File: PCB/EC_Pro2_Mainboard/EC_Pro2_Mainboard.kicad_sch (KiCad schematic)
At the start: 27 parts, among them J1 JST, J2 RGB, SW1 BOOT0, U1 STM32F401CBUx, U2 XC6206PxxxMR, U6 SN74AHCT1G125, Y1 8 MHz

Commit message: Updated sheets
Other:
- company: Cipulot PCB Design  -> LU.SV Solutions

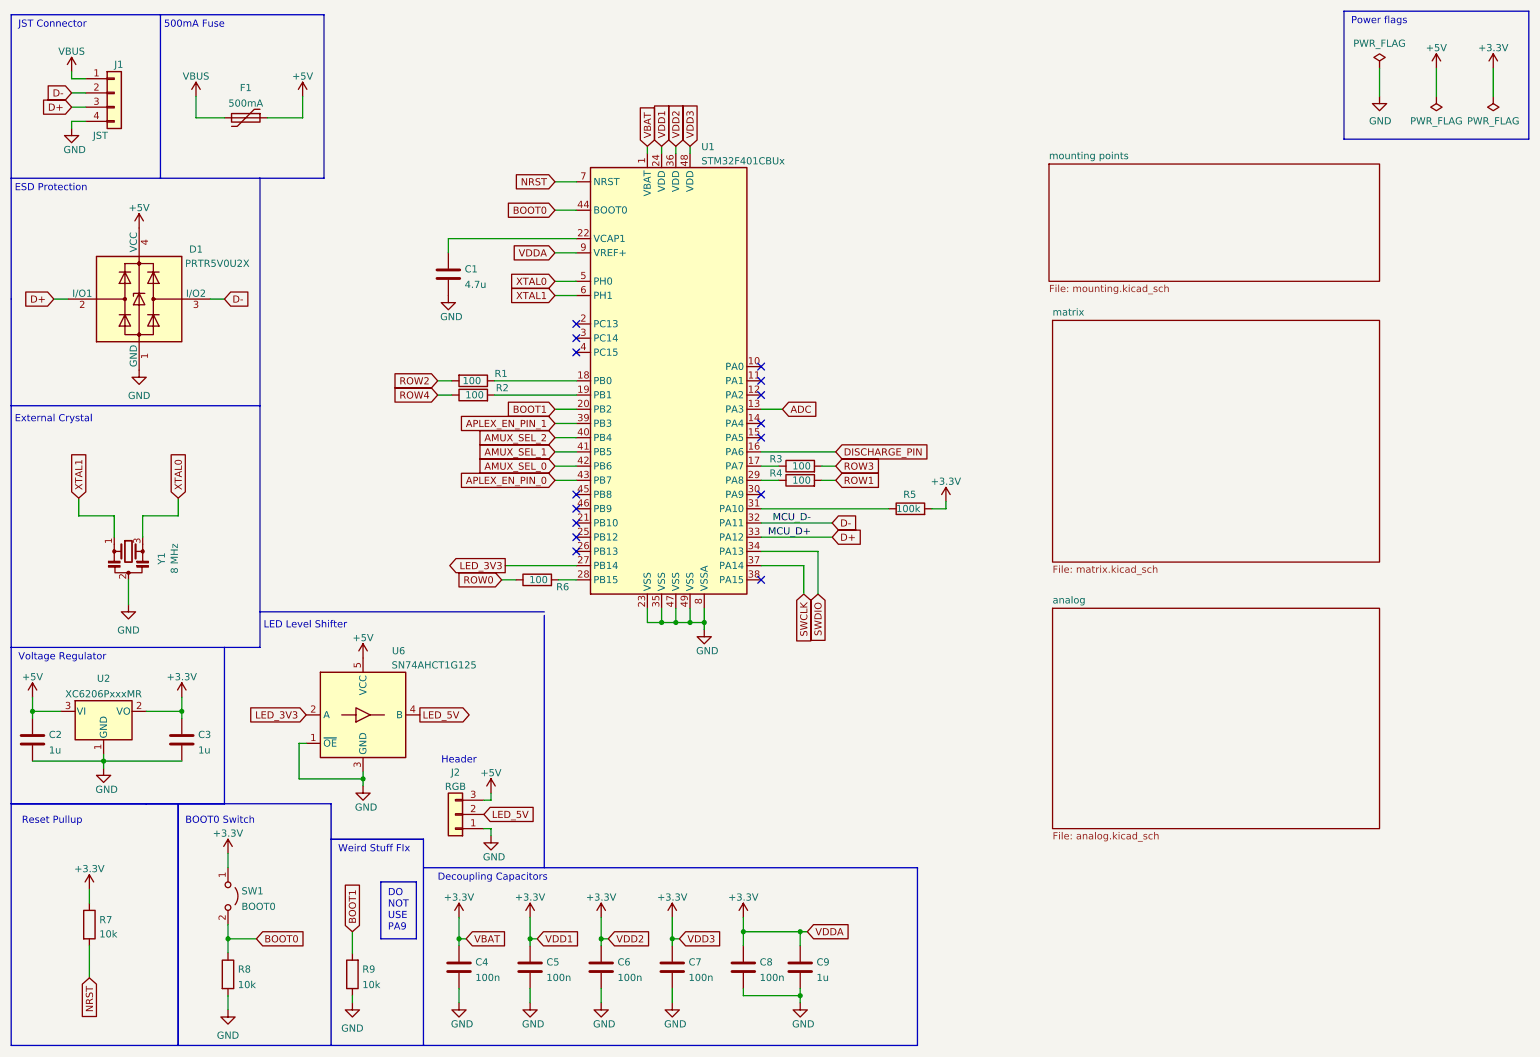
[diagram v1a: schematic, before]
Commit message: Update
Updated the License for the project and relative details.
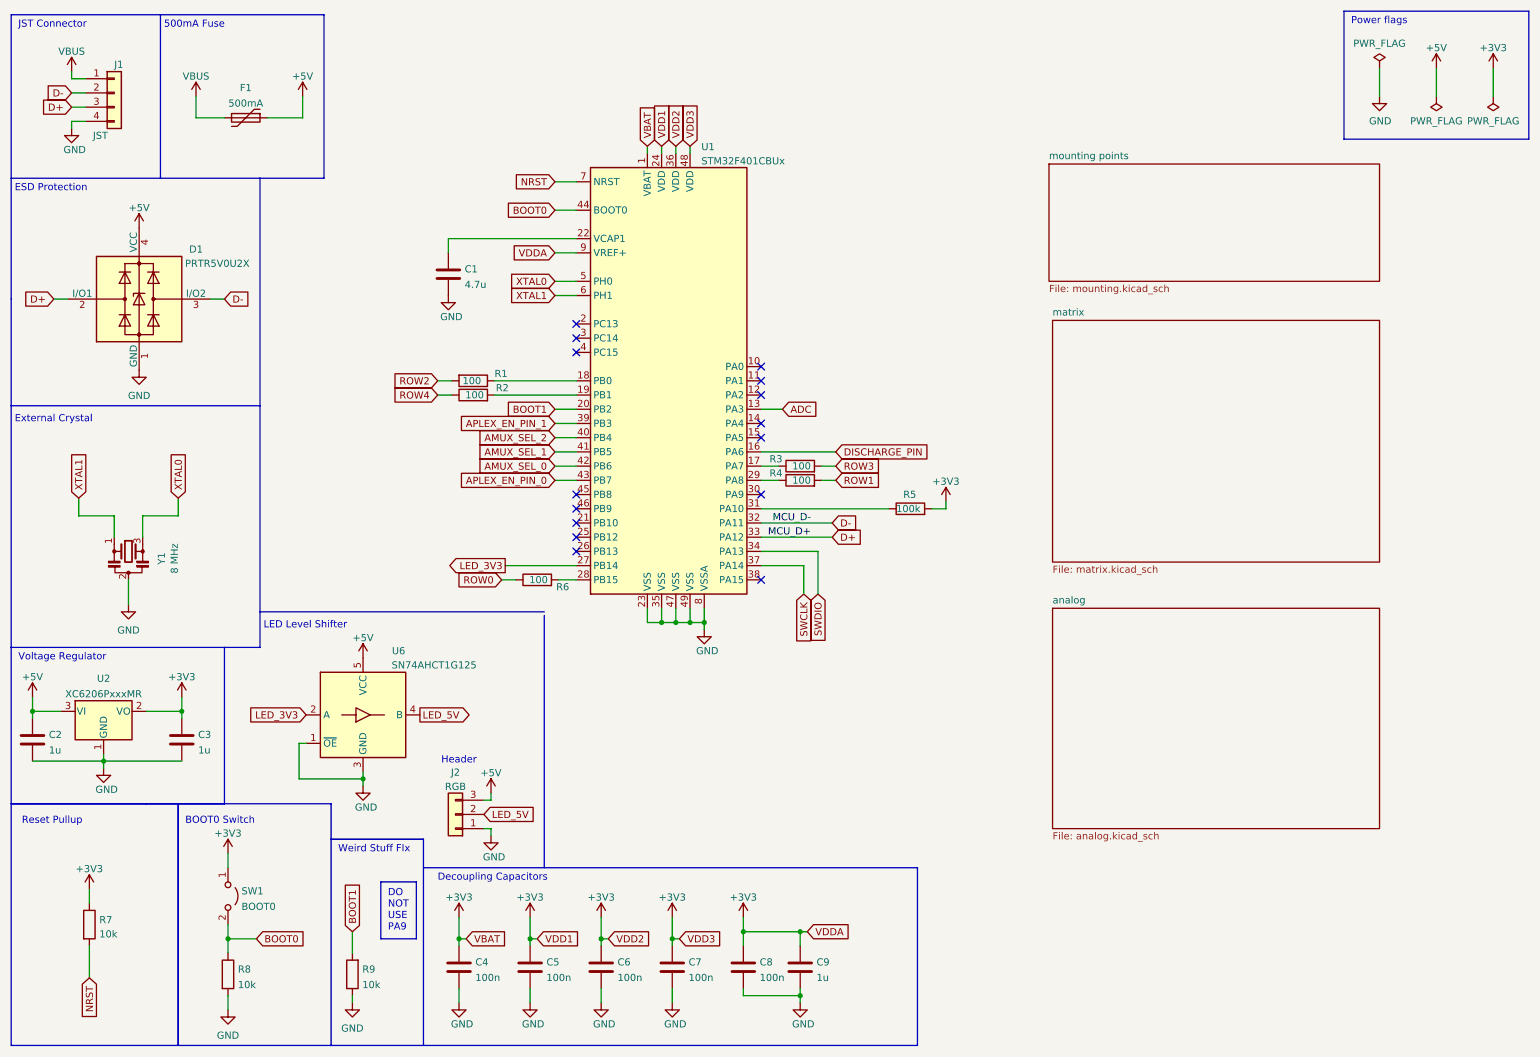
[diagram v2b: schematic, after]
